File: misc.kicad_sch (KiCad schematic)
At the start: 18 parts, among them U4 NTS0102_TSSOP, U5 NTS0102_TSSOP, Y1 Resonator_50MHz_XRCGE, Y2 Oscillator_25MHz_511ABA25M000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

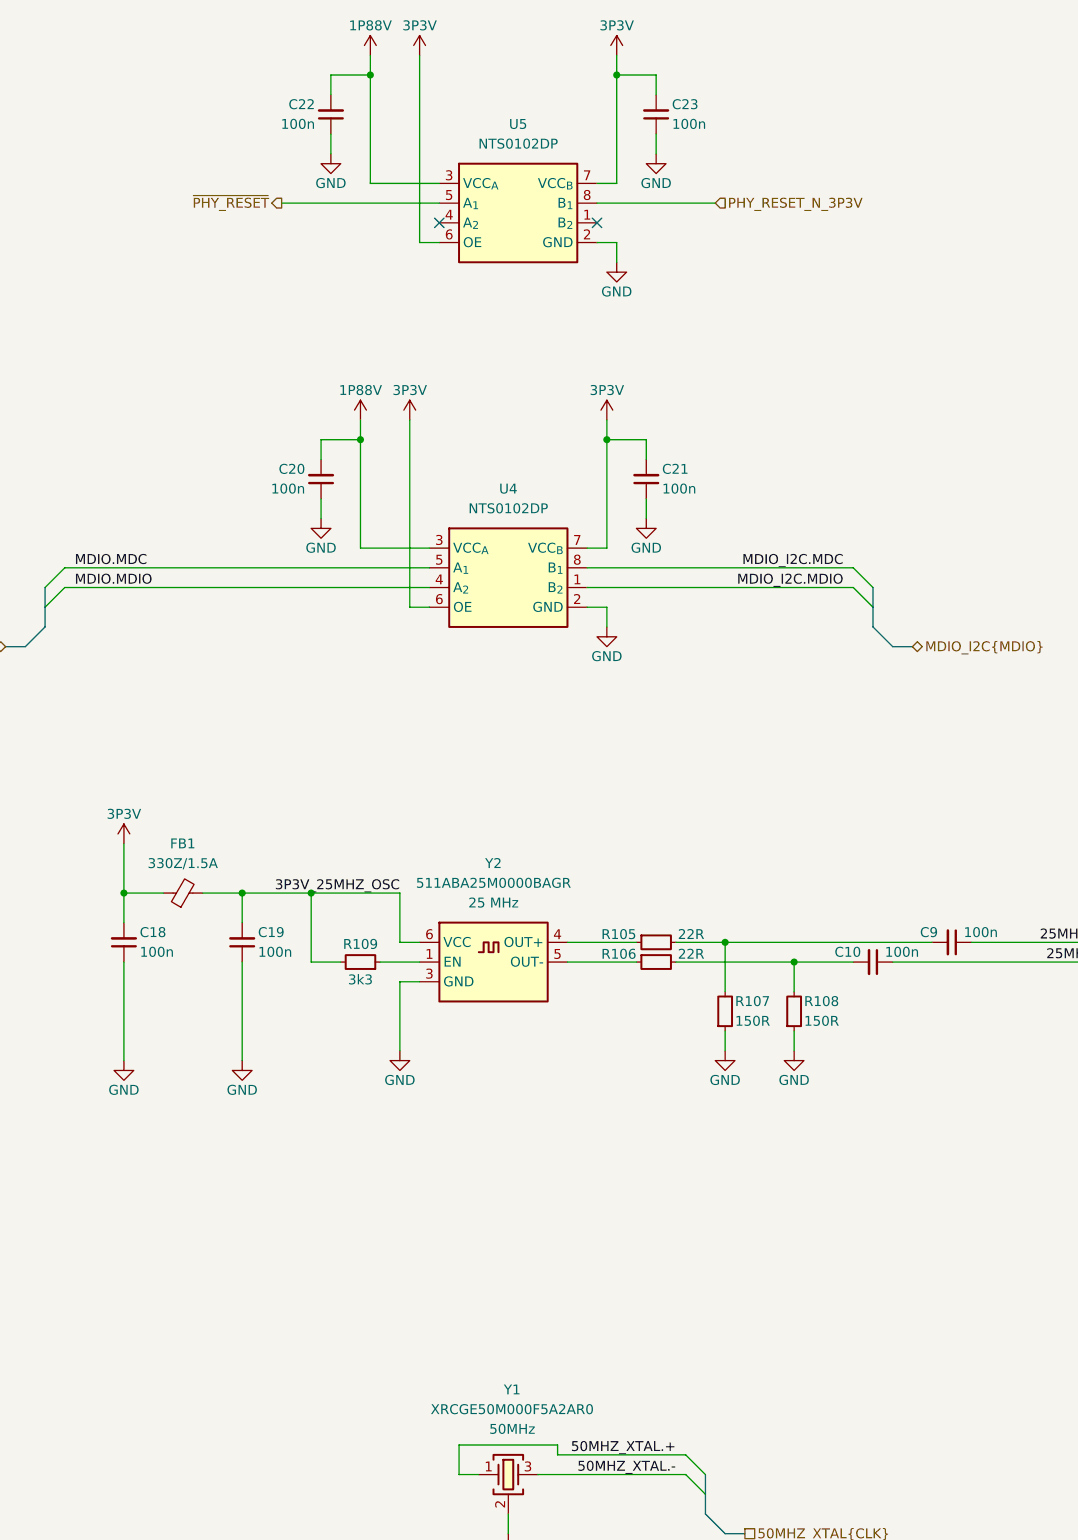
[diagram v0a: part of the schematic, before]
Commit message: [#80813] Change RJ45 connectors, reannotate schematics
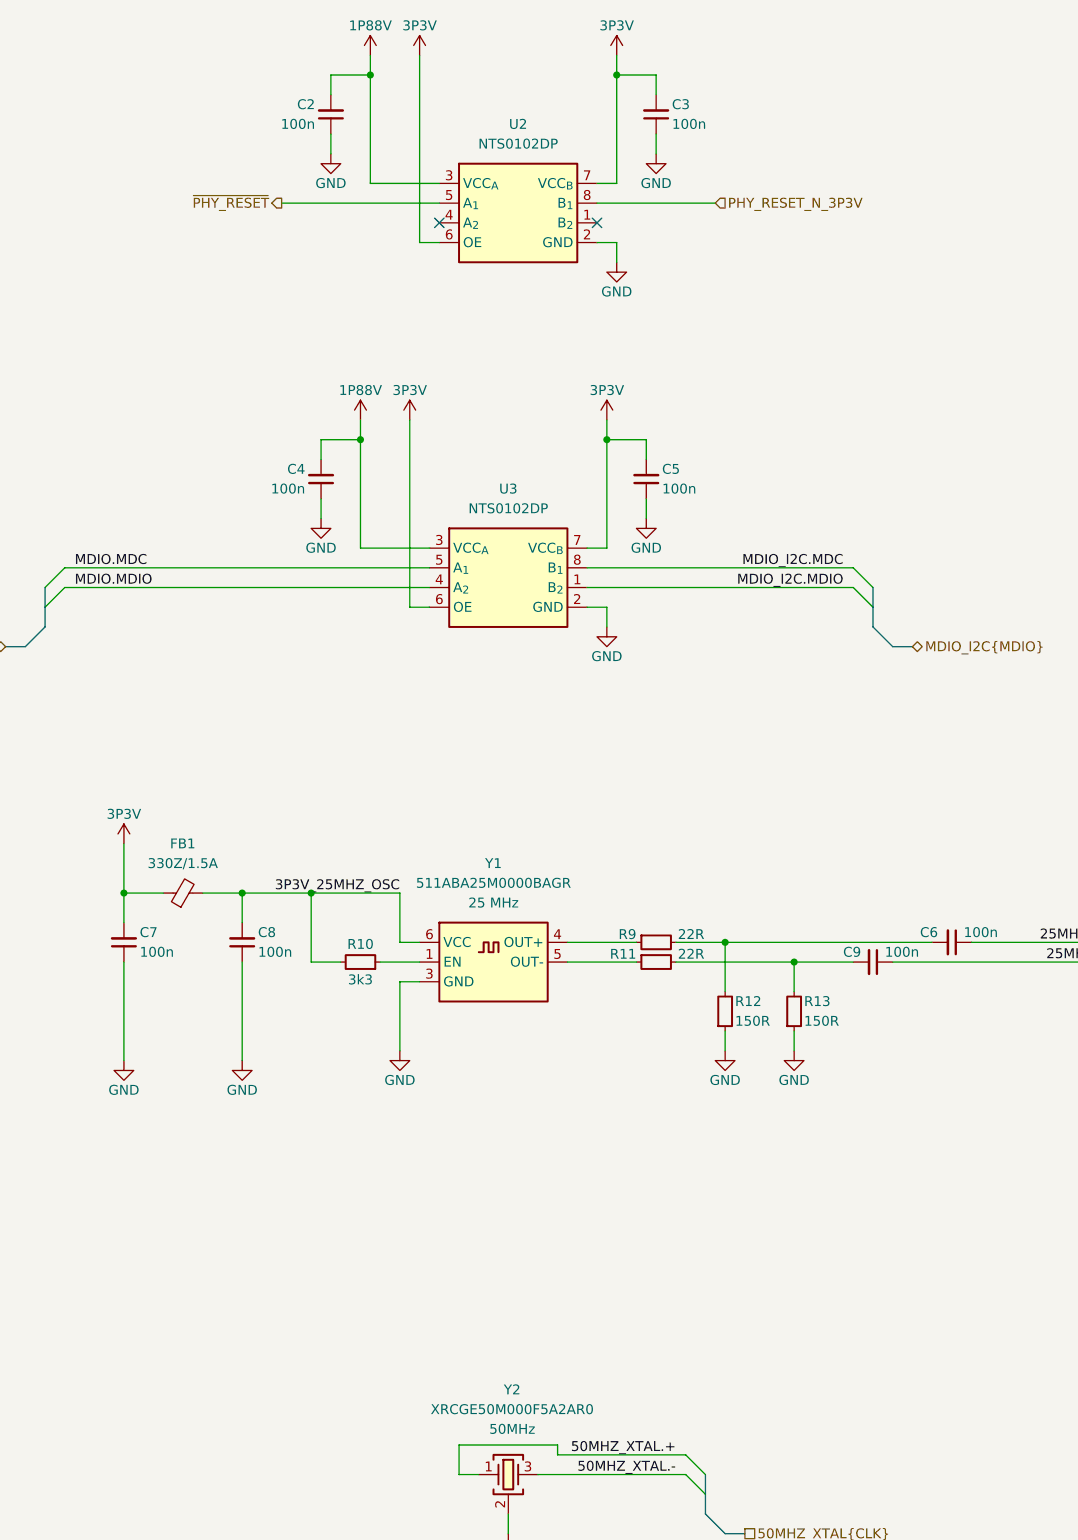
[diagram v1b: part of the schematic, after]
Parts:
- renumbered C22 to C2, C23 to C3, C20 to C4, C21 to C5, C9 to C6, C18 to C7, C19 to C8, C10 to C9, R109 to R10, R106 to R11, R107 to R12, R108 to R13, R105 to R9, U5 to U2, U4 to U3, Y2 to Y1, Y1 to Y2

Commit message: [#80813] Improve schematic readability, add debug connectors and missing resistors
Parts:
- added J4: PinSocket_2x11_P2.54mm_Drill1.02mm, antmicro-footprints:PinSocket_2x11_P2.54mm_Drill1.02mm, symbol antmicroGenericPinSockets:PinSocket_2x11_P2.54mm_Drill1.02mm
- added R124, R125, R126: R_0R_0402, antmicro-footprints:R_0402_1005Metric, symbol antmicroResistors0402:R_0R_0402
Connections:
- net GND: now also J4.10, J4.12, J4.2, J4.4, J4.6, J4.8, R124.1, R125.2, R126.1
- net at U2.1 (B_{2}): now also R125.1
- net at U2.4 (A_{2}): now also R126.2
- net PHY_RESET_N_3P3V renamed ~{PHY_RESET_3P3V}
- new net: J4.14, R124.2
- new net 12V_AUX_NCSI: J4.17, J4.18, J4.19, J4.20, J4.21
- new net NCSI_CONN.ARB_IN: J4.15
- new net NCSI_CONN.ARB_OUT: J4.16
- new net NCSI_CONN.CRS_DV: J4.3
- new net NCSI_CONN.REF_CLK: J4.1
- new net NCSI_CONN.RXD_0: J4.5
- new net NCSI_CONN.RXD_1: J4.7
- new net NCSI_CONN.TXD_0: J4.9
- new net NCSI_CONN.TXD_1: J4.11
- new net NCSI_CONN.TX_EN: J4.13
- no-connect marks 2 -> 1
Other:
- note added: "Crystal Oscillator And Resonator"
- note added: "NC-SI Debug Connector"
- note added: "Voltage Level Shifters"
- moved on the sheet: C2, C3, C4, C5, C6, C7, C8, C9, FB1, R10, R11, R12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

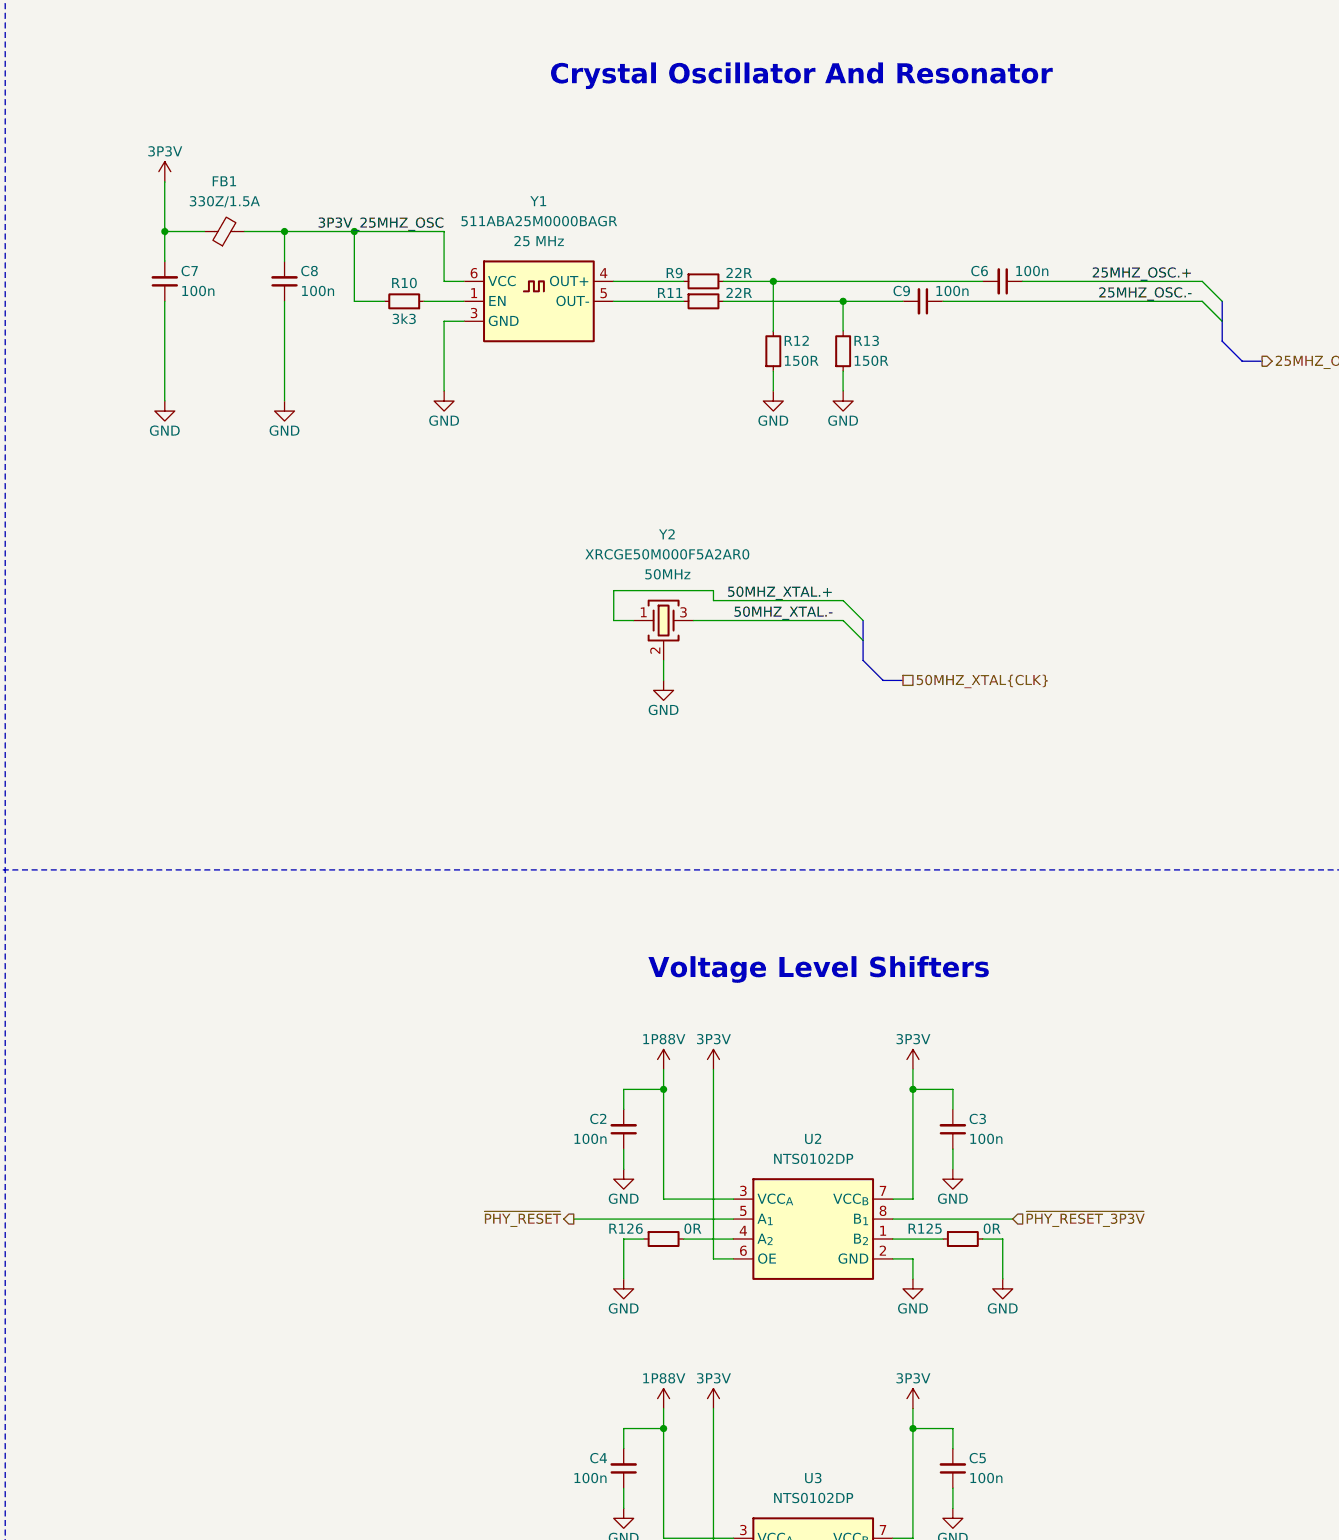
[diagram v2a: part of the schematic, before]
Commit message: [#80813] Change 3V3 and 1V88 power rails names
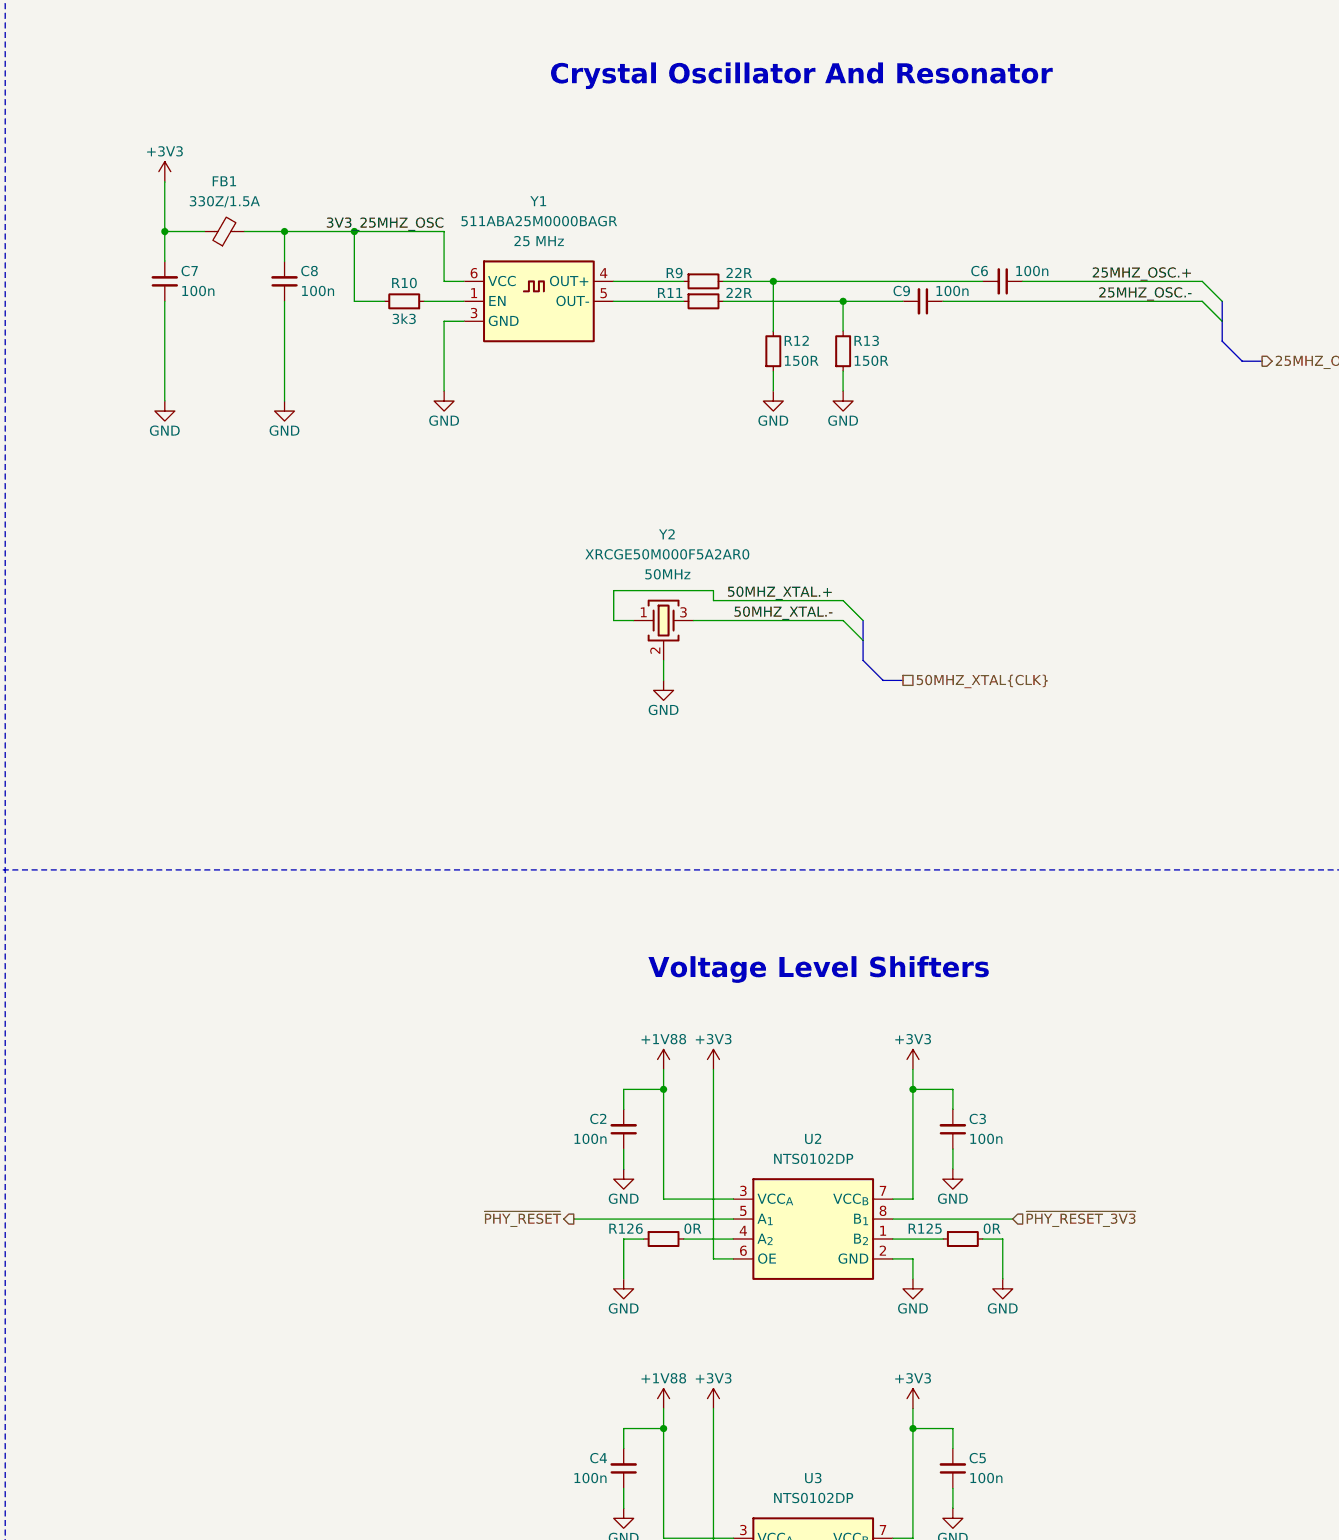
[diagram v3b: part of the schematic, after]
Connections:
- net 1P88V renamed +1V88
- net 3P3V renamed +3V3
- net 3P3V_25MHZ_OSC renamed 3V3_25MHZ_OSC
- net ~{PHY_RESET_3P3V} renamed ~{PHY_RESET_3V3}
